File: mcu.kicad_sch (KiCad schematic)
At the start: 24 parts

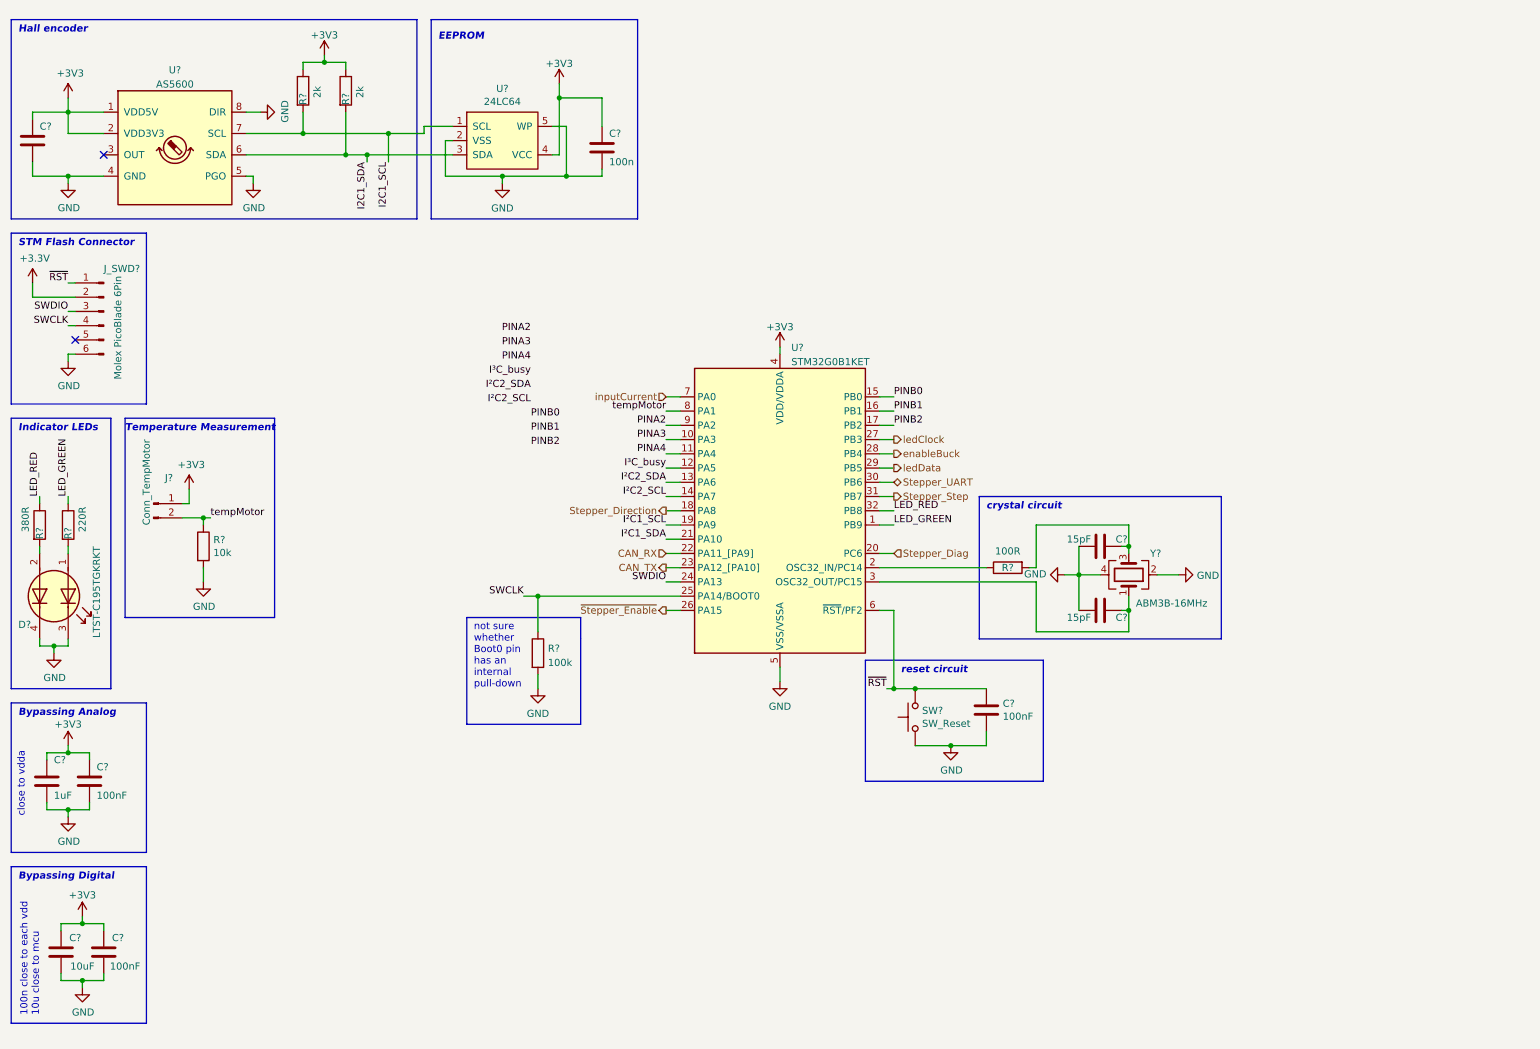
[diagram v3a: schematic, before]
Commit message: Annotate symbols and assign footprints
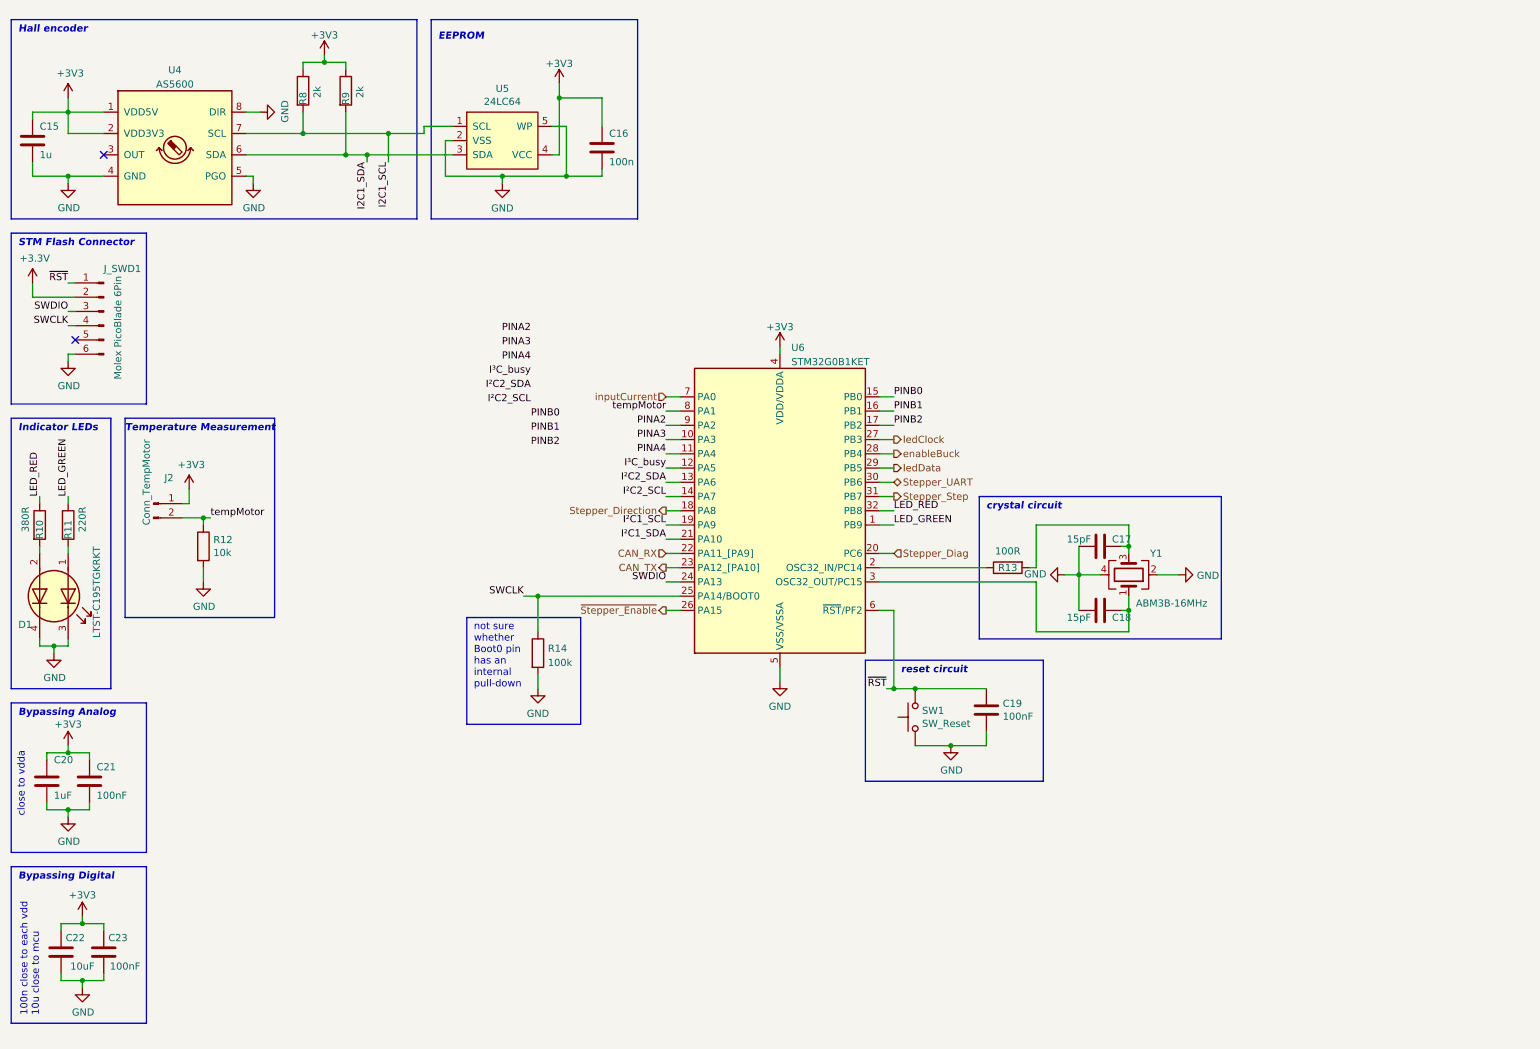
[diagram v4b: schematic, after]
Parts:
- C15: renamed from C?; value (none) -> 1u; footprint (none) -> Capacitor_SMD:C_0603_1608Metric
- U4: renamed from U?; footprint (none) -> Package_SO:SOIC-8_3.9x4.9mm_P1.27mm
- gave numbers to parts that had none: 22

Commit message: Finish schematic
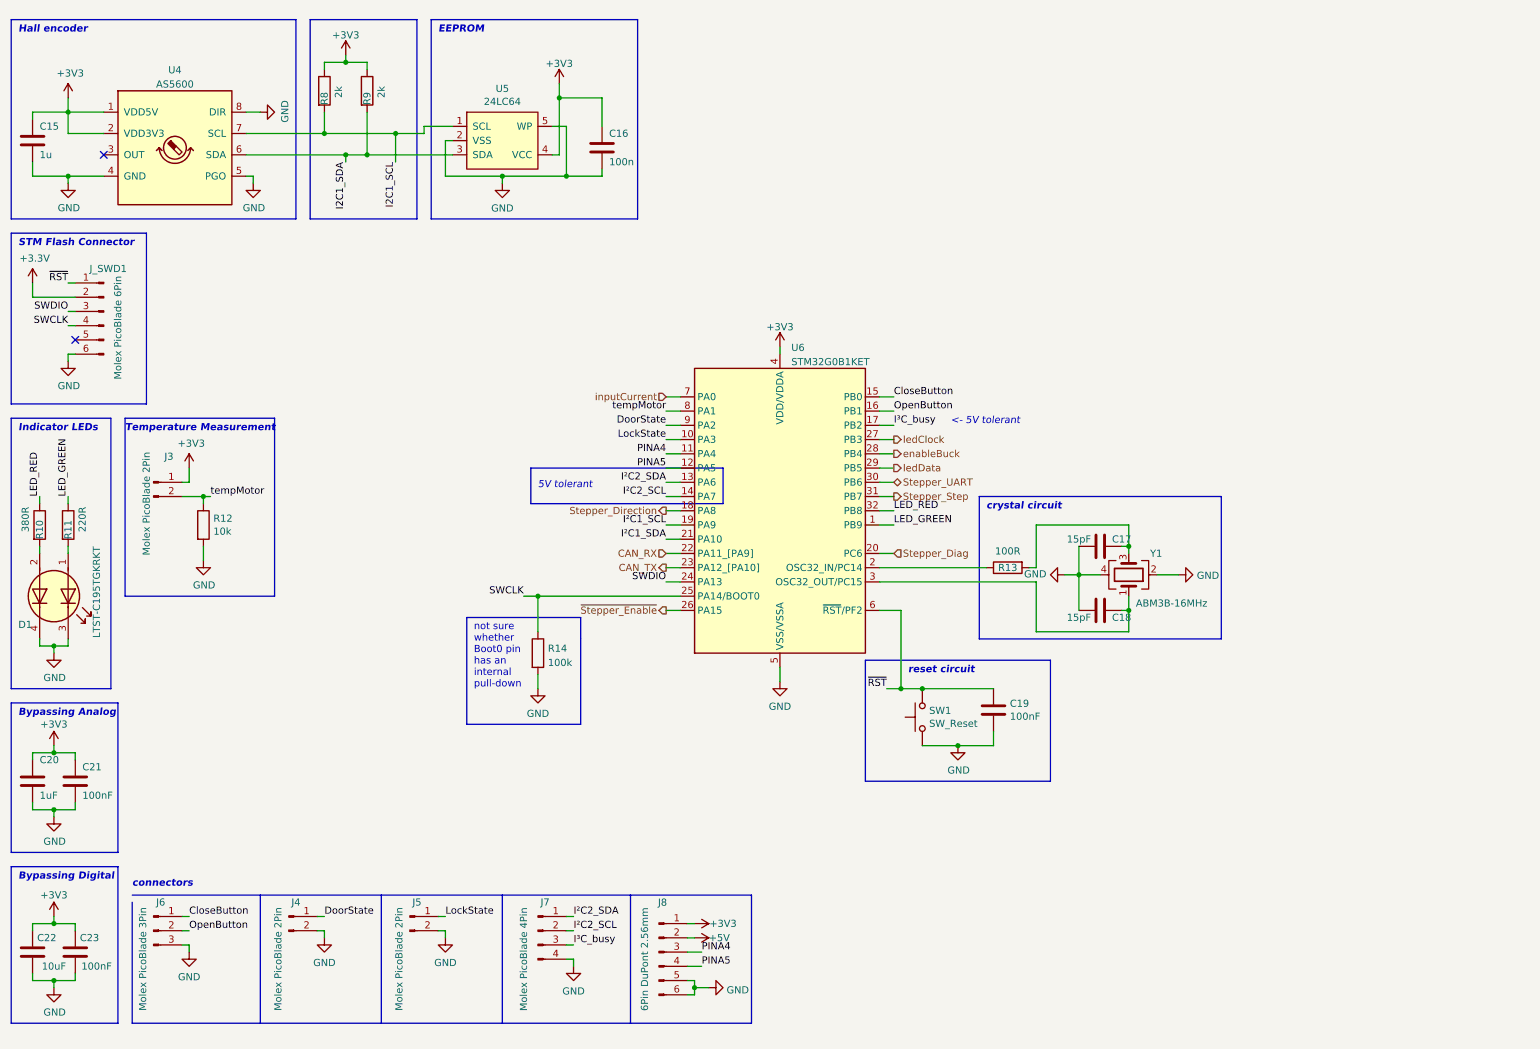
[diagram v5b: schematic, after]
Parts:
- added J4, J5: Molex PicoBlade 2Pin, Connector_Molex:Molex_PicoBlade_53047-0210_1x02_P1.25mm_Vertical, symbol Connector:Conn_01x02_Male
- added J6: Molex PicoBlade 3Pin, Connector_Molex:Molex_PicoBlade_53047-0310_1x03_P1.25mm_Vertical, symbol Connector:Conn_01x03_Male
- added J7: Molex PicoBlade 4Pin, Connector_Molex:Molex_PicoBlade_53047-0410_1x04_P1.25mm_Vertical, symbol Connector:Conn_01x04_Male
- added J8: 6Pin DuPont 2.56mm, Connector_PinHeader_2.54mm:PinHeader_1x06_P2.54mm_Vertical, symbol Connector:Conn_01x06_Male
- C16: footprint (none) -> Capacitor_SMD:C_0603_1608Metric
- J3: renamed from J2; value Conn_TempMotor -> Molex PicoBlade 2Pin
- R14: footprint (none) -> Resistor_SMD:R_0603_1608Metric
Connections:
- net PINB2 is gone; now on net I³C_busy: U6.17 (PB2)
- net +3V3: now also J8.1 (Pin_1)
- net GND: now also J4.2 (Pin_2), J5.2 (Pin_2), J6.3 (Pin_3), J7.4 (Pin_4), J8.5 (Pin_5), J8.6 (Pin_6)
- net I²C2_SCL: now also J7.2 (Pin_2)
- net I²C2_SDA: now also J7.1 (Pin_1)
- net I³C_busy: now also J7.3 (Pin_3); no longer U6.12 (PA5)
- net PINA4: now also J8.3 (Pin_3)
- net PINA2 renamed DoorState
- net DoorState: now also J4.1 (Pin_1)
- net PINA3 renamed LockState
- net LockState: now also J5.1 (Pin_1)
- net PINB0 renamed CloseButton
- net CloseButton: now also J6.1 (Pin_1)
- net PINB1 renamed OpenButton
- net OpenButton: now also J6.2 (Pin_2)
- new net +5V: J8.2 (Pin_2)
- new net PINA5: J8.4 (Pin_4), U6.12 (PA5)
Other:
- note added: "5V tolerant"
- note added: "<- 5V tolerant"
- note added: "connectors"
- note removed: "100n close to each vdd 10u close to mcu"
- note removed: "close to vdda"
- moved on the sheet: C19, C20, C21, C22, C23, J3, R12, R8, R9, SW1

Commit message: Add many changes to schematic and WIP PCB
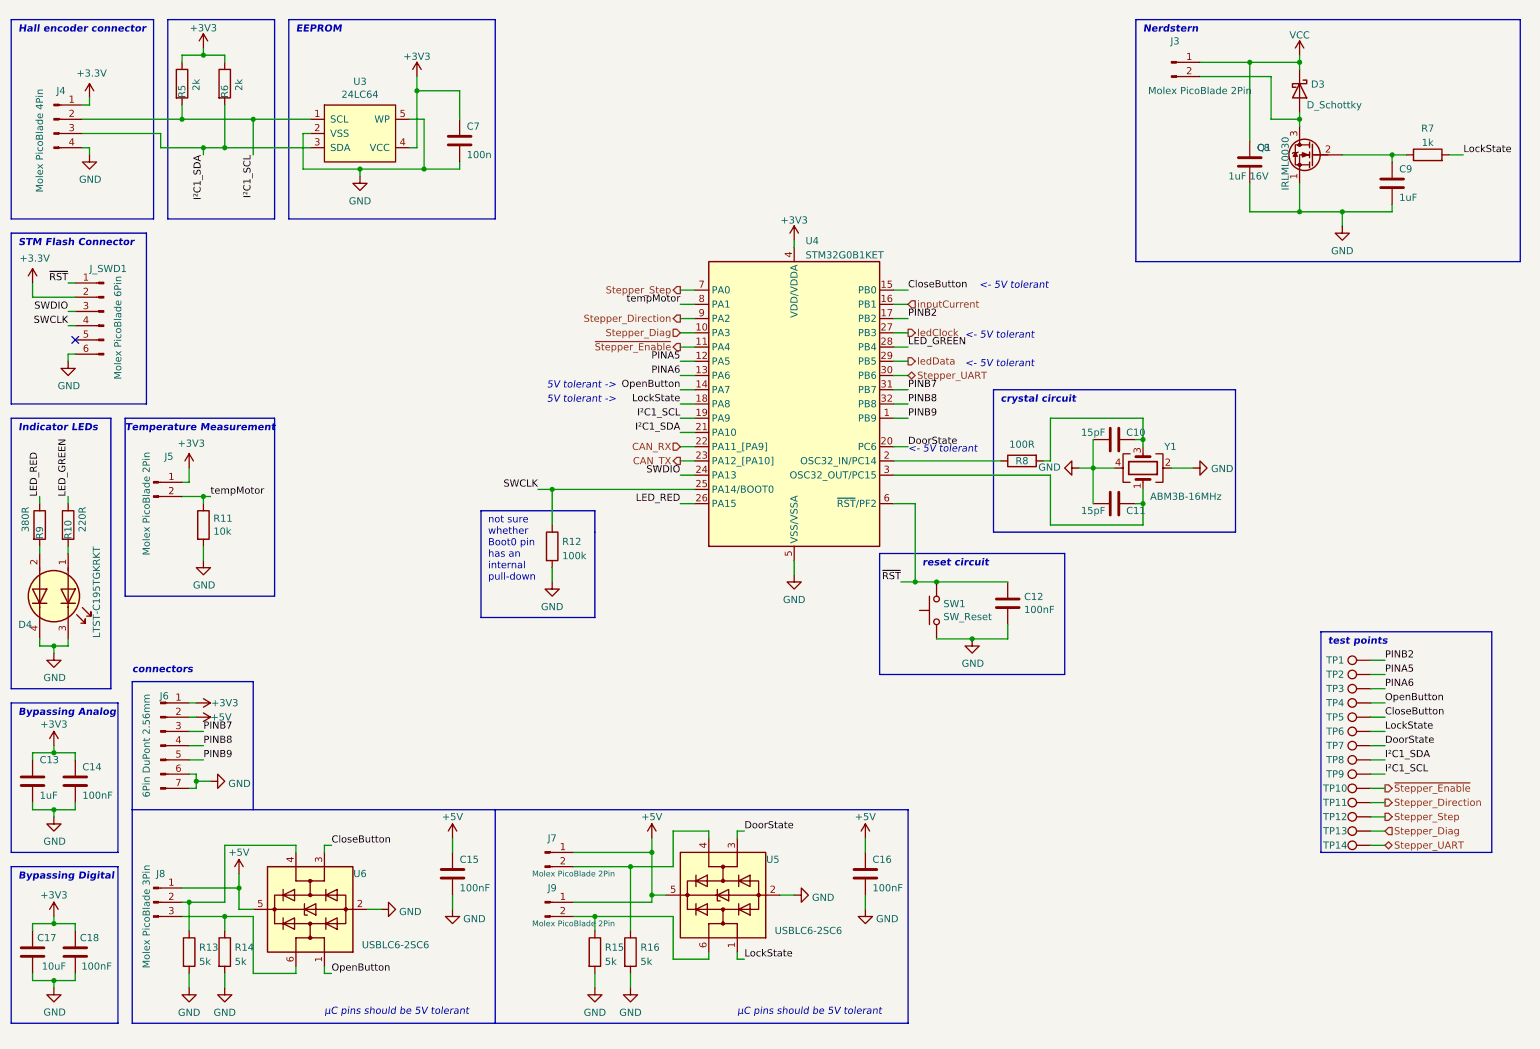
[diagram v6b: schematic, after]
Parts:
- removed J7: Molex PicoBlade 4Pin, Connector_Molex:Molex_PicoBlade_53047-0410_1x04_P1.25mm_Vertical, symbol Connector:Conn_01x04_Male
- removed U4: AS5600, Package_SO:SOIC-8_3.9x4.9mm_P1.27mm, symbol extraSymbols:AS5600
- added C16: 100nF, Capacitor_SMD:C_0603_1608Metric, symbol Device:C
- added C8: 1uF 16V, Capacitor_SMD:C_0603_1608Metric, symbol Device:C
- added C9: 1uF, Capacitor_SMD:C_0603_1608Metric, symbol Device:C
- added D3: D_Schottky, Diode_SMD:D_SOD-523, symbol Device:D_Schottky
- added J3: Molex PicoBlade 2Pin, Connector_Molex:Molex_PicoBlade_53047-0210_1x02_P1.25mm_Vertical, symbol Connector:Conn_01x02_Male
- added J4: Molex PicoBlade 4Pin, Connector_Molex:Molex_PicoBlade_53047-0410_1x04_P1.25mm_Vertical, symbol Connector:Conn_01x04_Male
- added Q1: IRLML0030, Package_TO_SOT_SMD:SOT-23, symbol Device:Q_NMOS_SGD
- added R13, R14, R15, R16: 5k, Resistor_SMD:R_0603_1608Metric, symbol Device:R
- added R7: 1k, Resistor_SMD:R_0603_1608Metric, symbol Device:R
- added TP1, TP10, TP11, TP12, TP13, TP14, TP2, TP3, TP4, TP5, TP6, TP7, TP8, TP9: TestPoint, TestPoint:TestPoint_Pad_D2.0mm, symbol Connector:TestPoint
- added U5, U6: USBLC6-2SC6, Package_TO_SOT_SMD:SOT-23-6, symbol Power_Protection:USBLC6-2SC6
- C15: value 1u -> 100nF
- J6: renamed from J8; footprint Connector_PinHeader_2.54mm:PinHeader_1x06_P2.54mm_Vertical -> Connector_PinHeader_2.54mm:PinHeader_1x07_P2.54mm_Vertical; symbol Connector:Conn_01x06_Male -> Connector:Conn_01x07_Male
- renumbered C17 to C10, C18 to C11, C19 to C12, C20 to C13, C21 to C14, C22 to C17, C23 to C18, C16 to C7, D1 to D4, J3 to J5, J4 to J7, J6 to J8, J5 to J9, R11 to R10, R12 to R11, R14 to R12, R8 to R5, R9 to R6, R13 to R8, R10 to R9, U5 to U3, U6 to U4
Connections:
- net I2C1_SCL is gone; now on net I²C1_SCL: R5.2, U3.1 (SCL)
- net I2C1_SDA is gone; now on net I²C1_SDA: R6.2, U3.3 (SDA)
- net I²C2_SCL is gone; now on net OpenButton: U4.14 (PA7)
- net enableBuck is gone; now on net LED_GREEN: U4.28 (PB4)
- net +3V3: now also J4.1 (Pin_1); no longer C15.1
- net +5V: now also C15.2, J7.1 (Pin_1), J8.1 (Pin_1), J9.1 (Pin_1), C16.2, U5.5 (VBUS), U6.5 (VBUS)
- net CloseButton: now also TP5.1, U6.3 (I/O2); no longer J8.1 (Pin_1)
- net DoorState: now also U4.20 (PC6), TP7.1, U5.3 (I/O2); no longer J7.1 (Pin_1), U4.9 (PA2)
- net GND: now also C15.1, J6.7 (Pin_7), C16.1, C8.2, C9.2, J4.4 (Pin_4), Q1.1 (S), R13.2, R14.2, R15.2, R16.2, U5.2 (GND), U6.2 (GND); no longer C15.2, J6.5 (Pin_5), J7.2 (Pin_2), J8.3 (Pin_3), J9.2 (Pin_2)
- net I²C1_SCL: now also J4.2 (Pin_2), TP9.1
- net I²C1_SDA: now also J4.3 (Pin_3), TP8.1
- net LED_GREEN: no longer U4.1 (PB9)
- net LED_RED: now also U4.26 (PA15); no longer U4.32 (PB8)
- net LockState: now also U4.18 (PA8), R7.2, TP6.1, U5.1 (I/O1); no longer J9.1 (Pin_1), U4.10 (PA3)
- net OpenButton: now also TP4.1, U6.1 (I/O1); no longer J8.2 (Pin_2), U4.16 (PB1)
- net PINA5: now also TP2.1; no longer J6.4 (Pin_4)
- net Stepper_Diag: now also U4.10 (PA3), TP13.1; no longer U4.20 (PC6)
- net Stepper_Direction: now also U4.9 (PA2), TP11.1; no longer U4.18 (PA8)
- net Stepper_Step: now also U4.7 (PA0), TP12.1; no longer U4.31 (PB7)
- net Stepper_UART: now also TP14.1
- net inputCurrent: now also U4.16 (PB1); no longer U4.7 (PA0)
- net ~{Stepper_Enable}: now also U4.11 (PA4), TP10.1; no longer U4.26 (PA15)
- net I²C2_SDA renamed PINA6
- net PINA6: now also TP3.1
- net I³C_busy renamed PINB2
- net PINB2: now also TP1.1
- net PINA4 renamed PINB7
- net PINB7: now also U4.31 (PB7); no longer U4.11 (PA4)
- new net: C9.1, Q1.2 (G), R7.1
- new net: J8.2 (Pin_2), R13.1, U6.4 (I/O2)
- new net: J8.3 (Pin_3), R14.1, U6.6 (I/O1)
- new net: J9.2 (Pin_2), R15.1, U5.6 (I/O1)
- new net: D3.2 (A), J3.2 (Pin_2), Q1.3 (D)
- new net: J7.2 (Pin_2), R16.1, U5.4 (I/O2)
- new net PINB8: J6.4 (Pin_4), U4.32 (PB8)
- new net PINB9: J6.5 (Pin_5), U4.1 (PB9)
- new net VCC: C8.1, D3.1 (K), J3.1 (Pin_1)
- no-connect marks 2 -> 1
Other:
- note added: "5V tolerant ->"
- note added: "Hall encoder connector"
- note added: "Nerdstern"
- note added: "test points"
- note added: "µC pins should be 5V tolerant"
- note removed: "5V tolerant"
- note removed: "Hall encoder"
- moved on the sheet: C10, C11, C12, C7, J7, J8, J9, R12, R5, R6, R8, SW1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
